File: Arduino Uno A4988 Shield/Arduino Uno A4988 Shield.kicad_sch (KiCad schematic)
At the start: 1 part

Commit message: added template
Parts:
- removed A1: Arduino_UNO_R3, Module:Arduino_UNO_R3, symbol MCU_Module:Arduino_UNO_R3
- added A1: Pololu_Breakout_A4988, Module:Pololu_Breakout-16_15.2x20.3mm, symbol Driver_Motor:Pololu_Breakout_A4988
- added J1: Power, Connector_PinSocket_2.54mm:PinSocket_1x08_P2.54mm_Vertical, symbol Connector_Generic:Conn_01x08
- added J2: Digital/PWM, Connector_PinSocket_2.54mm:PinSocket_1x10_P2.54mm_Vertical, symbol Connector_Generic:Conn_01x10
- added J3: Analog, Connector_PinSocket_2.54mm:PinSocket_1x06_P2.54mm_Vertical, symbol Connector_Generic:Conn_01x06
- added J4: Digital/PWM, Connector_PinSocket_2.54mm:PinSocket_1x08_P2.54mm_Vertical, symbol Connector_Generic:Conn_01x08
- added J5: Conn_01x04, Connector_PinHeader_2.54mm:PinHeader_1x04_P2.54mm_Vertical, symbol Connector_Generic:Conn_01x04
- added SW1: SW_DIP_x03, Button_Switch_SMD:SW_DIP_SPSTx03_Slide_9.78x9.8mm_W8.61mm_P2.54mm, symbol Switch:SW_DIP_x03
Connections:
- new net: A1.12 (MS3), SW1.1
- new net: A1.11 (MS2), SW1.2
- new net: A1.10 (MS1), SW1.3
- new net: A1.3 (1B), J5.1 (Pin_1)
- new net: A1.4 (1A), J5.2 (Pin_2)
- new net: A1.5 (2A), J5.3 (Pin_3)
- new net: A1.6 (2B), J5.4 (Pin_4)
- new net *10: J2.8 (Pin_8)
- new net *11: J2.7 (Pin_7)
- new net *3: J4.5 (Pin_5)
- new net *5: J4.3 (Pin_3)
- new net *6: J4.2 (Pin_2)
- new net *9: J2.9 (Pin_9)
- new net +3V3: J1.4 (Pin_4)
- new net +5V: J1.5 (Pin_5), SW1.4, SW1.5, SW1.6
- new net 12: J2.6 (Pin_6)
- new net 13: J2.5 (Pin_5)
- new net 2: J4.6 (Pin_6)
- new net 4: J4.4 (Pin_4)
- new net 7: J4.1 (Pin_1)
- new net 8: J2.10 (Pin_10)
- new net 9: A1.15 (STEP)
- new net A0: J3.1 (Pin_1)
- new net A1: J3.2 (Pin_2)
- new net A2: J3.3 (Pin_3)
- new net A3: J3.4 (Pin_4)
- new net AREF: J2.3 (Pin_3)
- new net GND: J1.6 (Pin_6), J1.7 (Pin_7), J2.4 (Pin_4)
- new net IOREF: J1.2 (Pin_2)
- new net RX/0: J4.8 (Pin_8)
- new net SCL/A5: J2.1 (Pin_1), J3.6 (Pin_6)
- new net SDA/A4: J2.2 (Pin_2), J3.5 (Pin_5)
- new net TX/1: J4.7 (Pin_7)
- new net VCC: J1.8 (Pin_8)
- new net ~{RESET}: J1.3 (Pin_3)
- no-connect marks 0 -> 1
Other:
- note added: "* Indicates a PWM-capable pin"

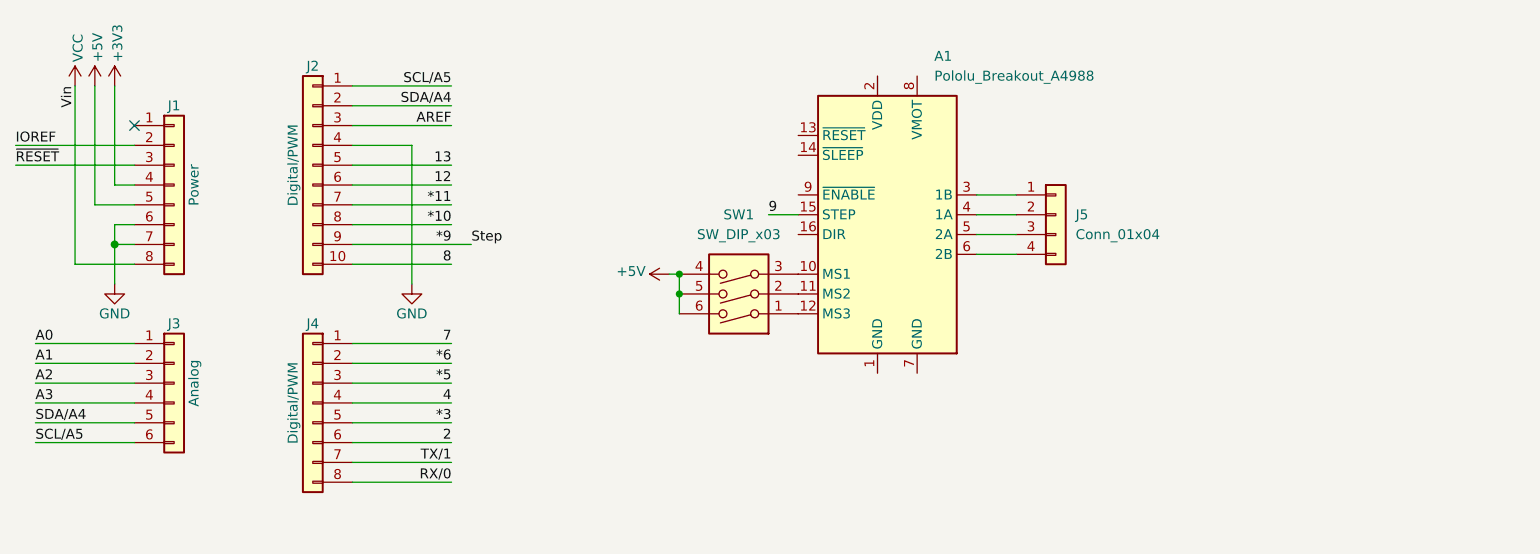
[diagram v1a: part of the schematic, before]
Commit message: Completed Shaorong and A4988 Shield
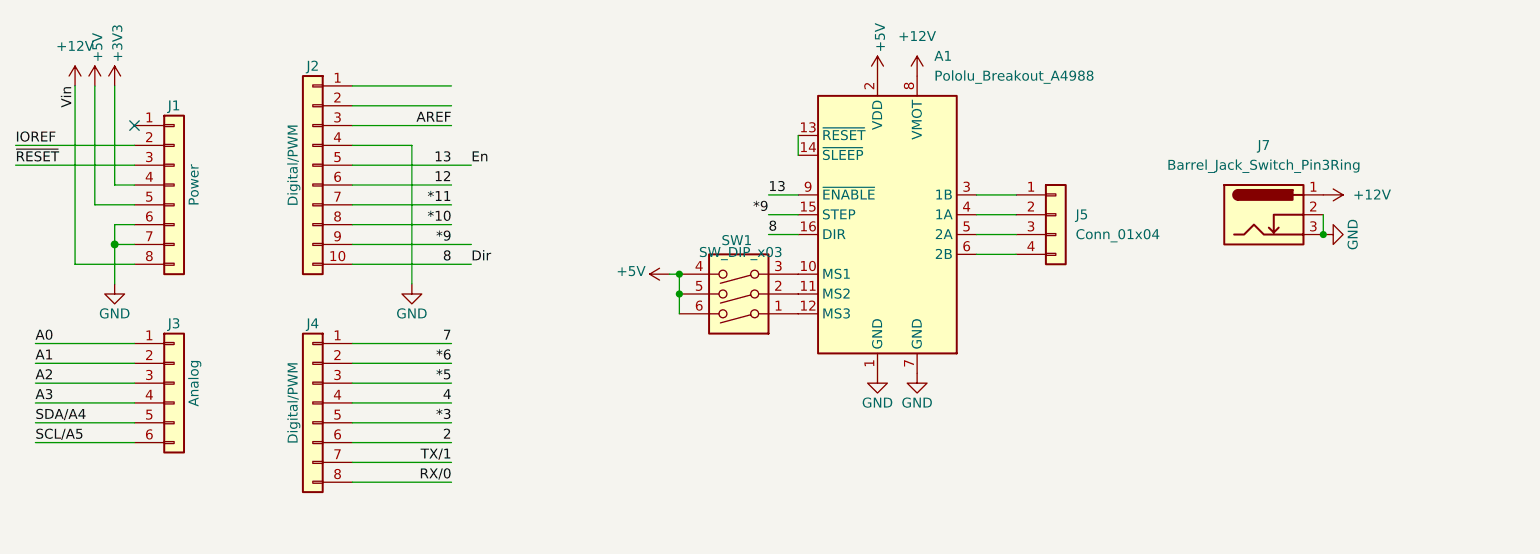
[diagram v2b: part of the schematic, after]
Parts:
- added J7: Barrel_Jack_Switch_Pin3Ring, Connector_BarrelJack:BarrelJack_GCT_DCJ200-10-A_Horizontal, symbol Connector:Barrel_Jack_Switch_Pin3Ring
- SW1: footprint Button_Switch_SMD:SW_DIP_SPSTx03_Slide_9.78x9.8mm_W8.61mm_P2.54mm -> Button_Switch_SMD:SW_DIP_SPSTx03_Slide_6.7x9.18mm_W8.61mm_P2.54mm_LowProfile
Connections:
- net 9 is gone; now on net *9: A1.15 (STEP)
- net VCC is gone; now on net +12V: J1.8 (Pin_8)
- net +5V: now also A1.2 (VDD)
- net 13: now also A1.9 (~{ENABLE})
- net 8: now also A1.16 (DIR)
- net GND: now also A1.1 (GND), A1.7 (GND), J7.2, J7.3
- net SCL/A5: no longer J2.1 (Pin_1)
- net SDA/A4: no longer J2.2 (Pin_2)
- net at A1.13 (~{RESET}): now also A1.14 (~{SLEEP})
- net +12V: now reaches A1.8 (VMOT)
- net +12V: now also J7.1
